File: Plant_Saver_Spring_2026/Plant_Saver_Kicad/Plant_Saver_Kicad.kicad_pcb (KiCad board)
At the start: 2 copper layers, 110 parts, among them J10 DM3D-SF, J11 Test, J2 SBH11-PBPC-D05-ST-BK, J3 SM04B-SRSS-TB, J5 Conn_01x02_Pin, J6 Conn_01x06_Socket, J7 S3B-PH-K-S, J8 54-00284, J9 1.25mm, Q1 G09P02L, Q10 G09P02L, Q11 ISP12DP06NMXTSA1, Q12 G09P02L, Q2 G09P02L, Q3 ISP12DP06NMXTSA1, Q4 G09P02L, Q5 G09P02L, Q6 G09P02L, Q7 G09P02L, Q8 G09P02L, Q9 G09P02L, SW1 Reset, SW2 25336NA, SW3 Boot, SW4 SA72SB0, U1 CDBA140SL-HF, U10 DW03C, U11 CDBA140SL-HF, U12 LP38511TJ-ADJ/NOPB, U13 MCP73833-xxx-UN, U14 MCP6234, U15 MCP73833-xxx-UN, U16 MCP6547T_I_MS, U2 CDBA140SL-HF, U3 CDBA140SL-HF, U4 CDBA140SL-HF, U5 ESP32-WROOM-32E-N16, U9 CDBA140SL-HF

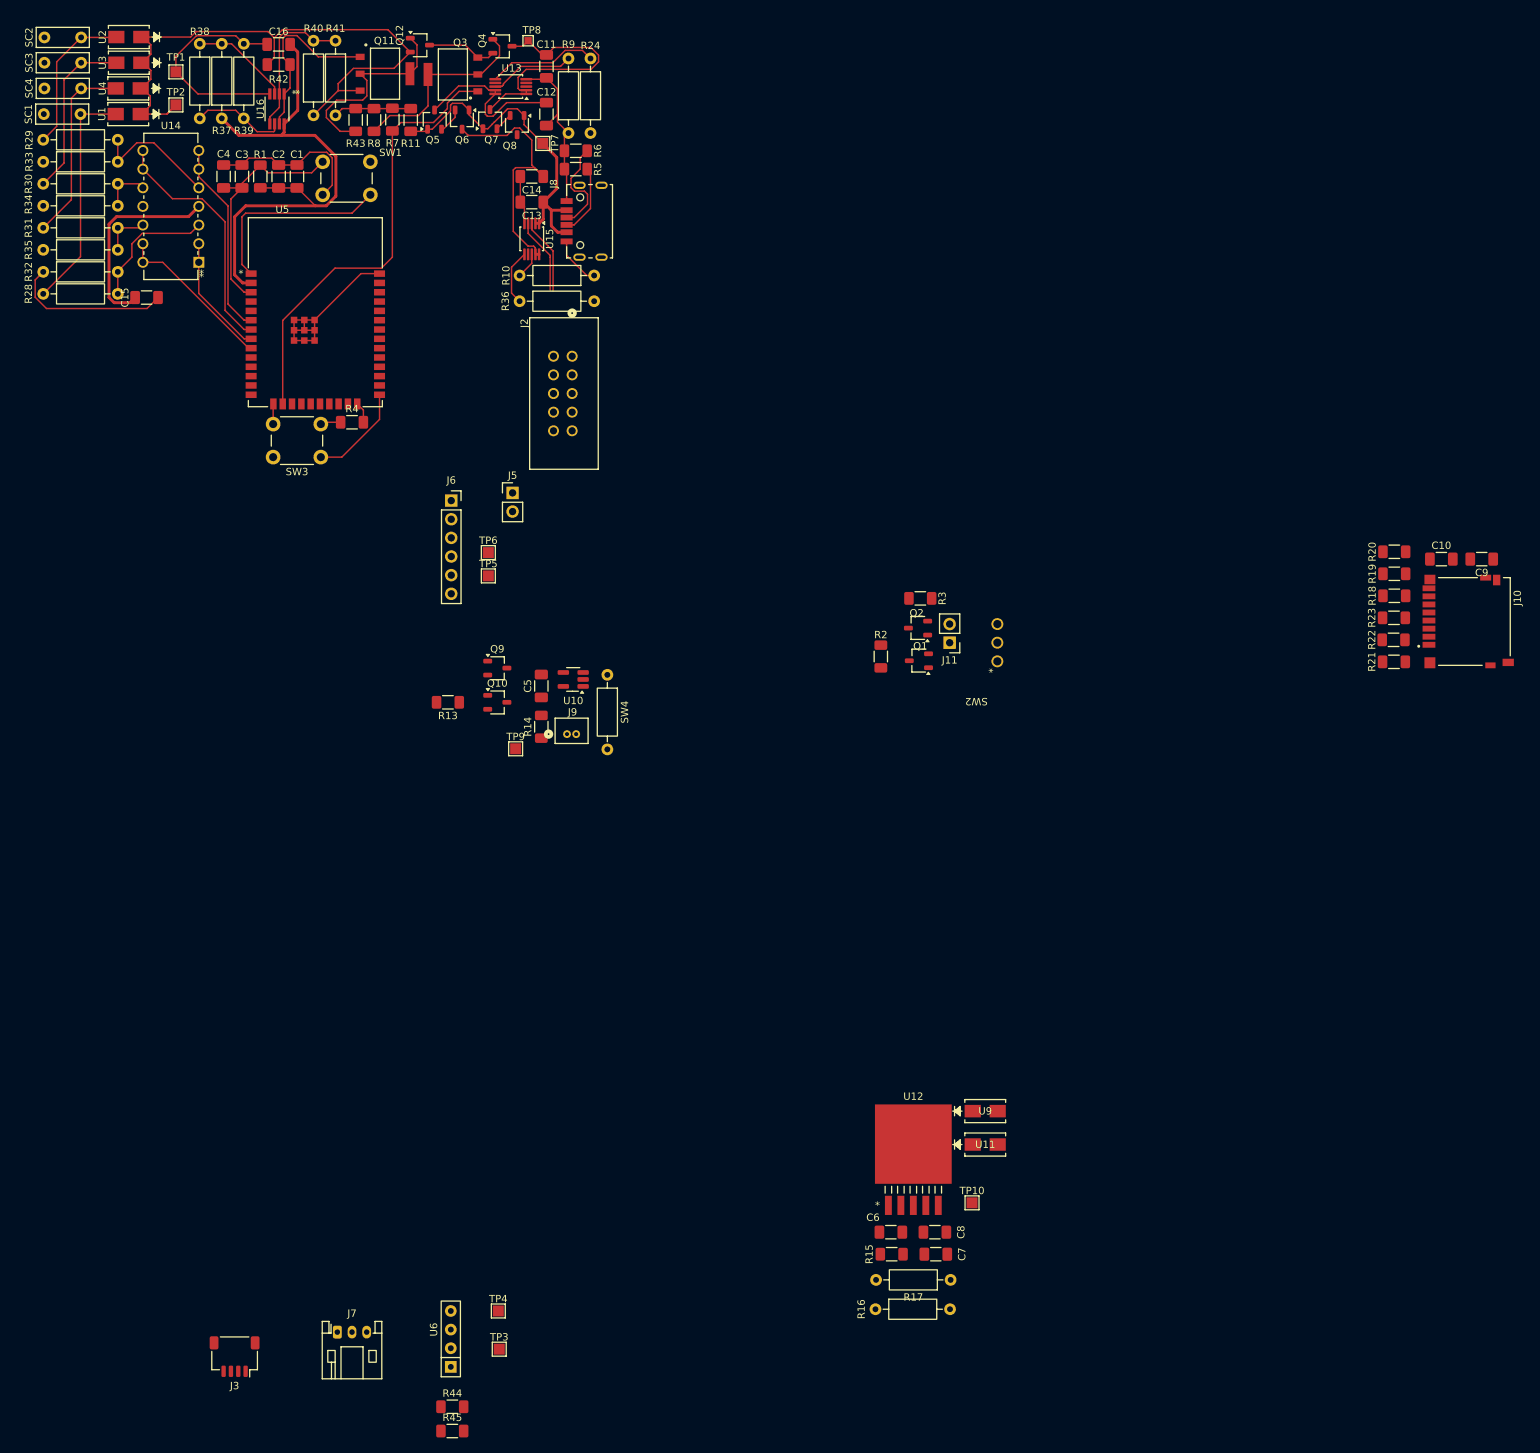
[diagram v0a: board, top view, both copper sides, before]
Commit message: Charge circuit essentially added to pcb
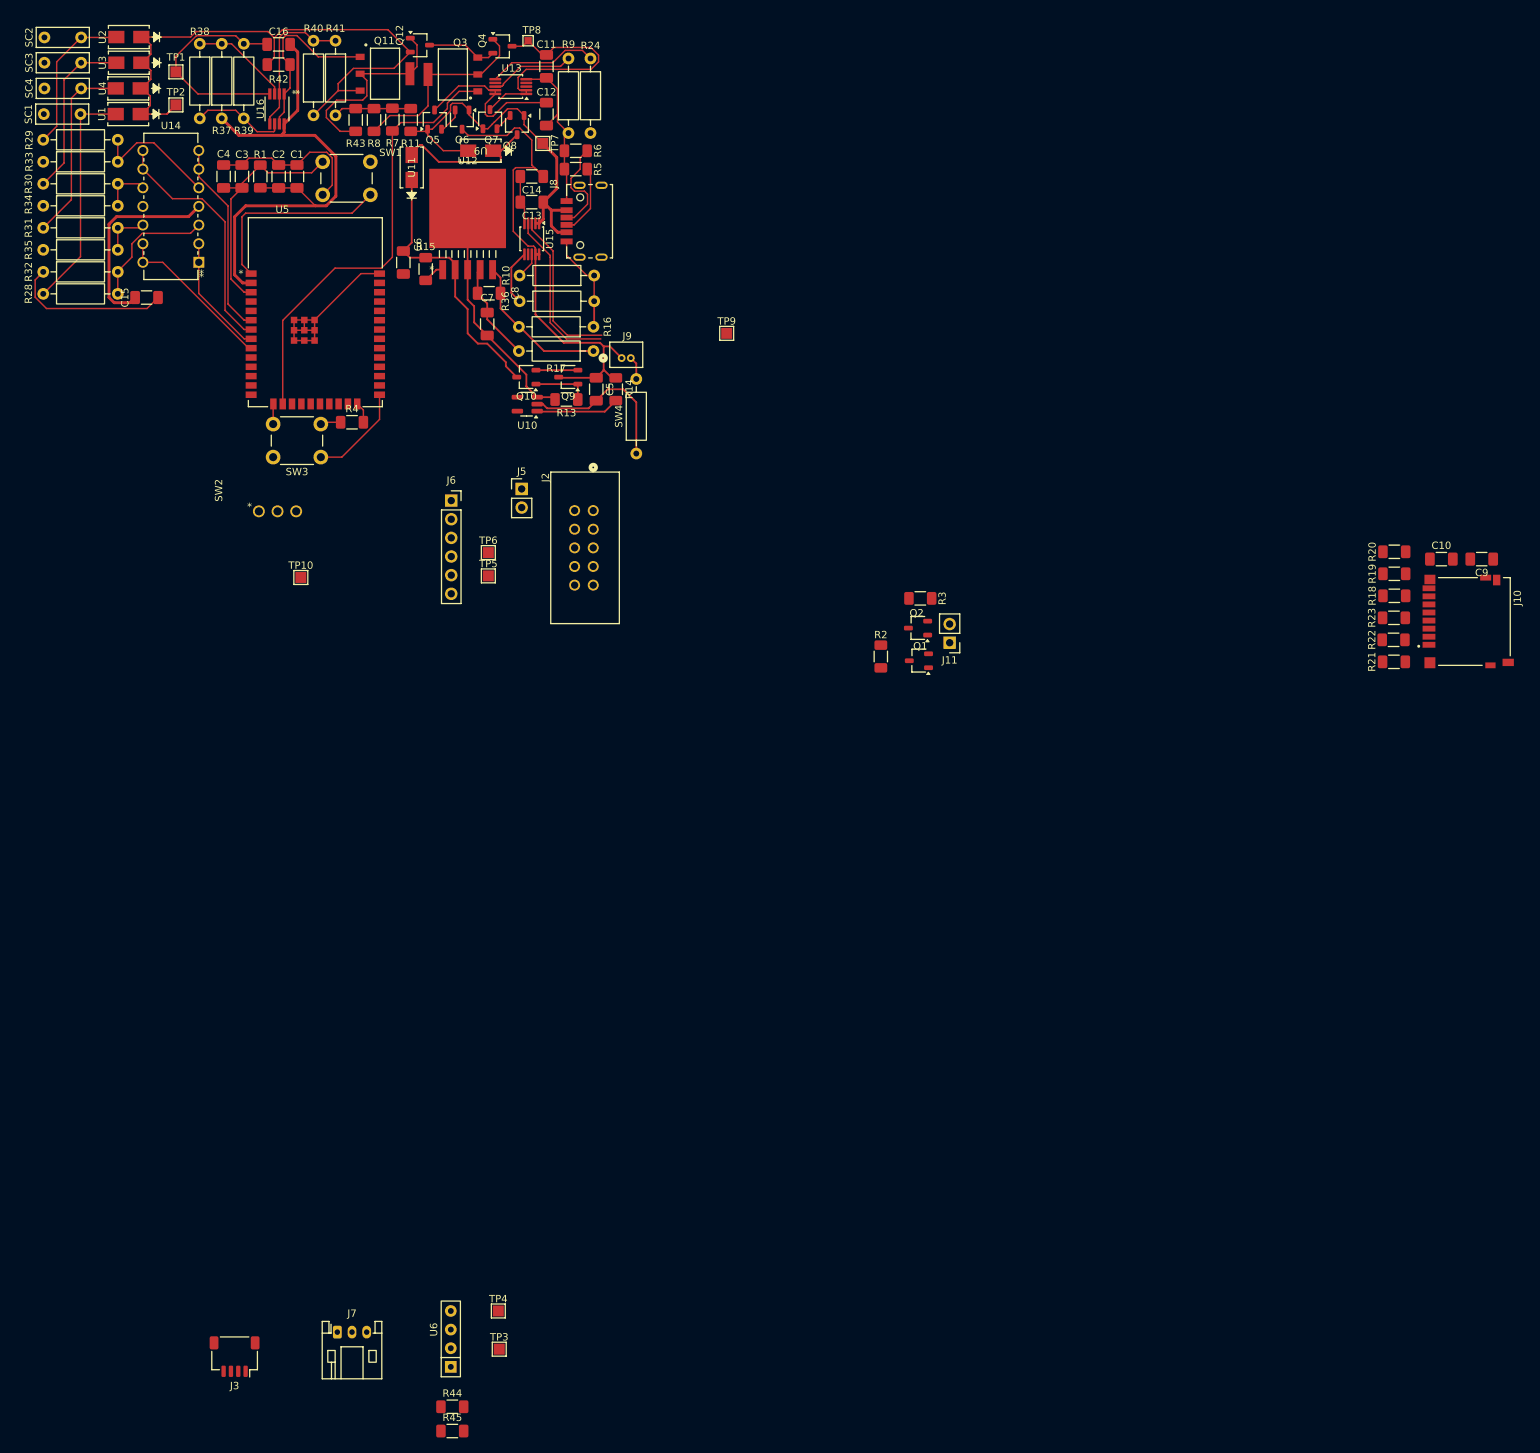
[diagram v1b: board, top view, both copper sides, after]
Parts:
- moved U11 154.4 mm to (80.1, 88.8), turned to 90 degrees
- moved R15 148.5 mm to (82.0, 102.6), turned to 90 degrees
- moved C6 147.9 mm to (79.0, 101.7), turned to -90 degrees
- moved U9 147.9 mm to (89.5, 86.5), turned to 180 degrees
- moved C8 141.7 mm to (90.7, 105.9)
- moved U12 141.2 mm to (87.8, 94.4)
- moved C7 140.7 mm to (90.4, 110.1), turned to -90 degrees
- moved R16 139.3 mm to (104.9, 110.5), turned to 180 degrees
- moved R17 135.6 mm to (104.9, 113.8)
- moved TP10 125.0 mm to (65.0, 144.7)
- moved SW2 102.7 mm to (59.3, 135.6), turned to 0 degrees
- moved TP9 63.5 mm to (123.1, 111.4)
- moved J9 51.8 mm to (108.7, 114.8)
- moved R14 47.1 mm to (108.0, 119.0), turned to -90 degrees
- moved Q10 44.5 mm to (95.8, 117.3), turned to 180 degrees
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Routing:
- net GND: track 181.2 -> 220.5 mm
- net /Power_And_Charging/Linear_Regulator/Vin: track 0.00 -> 37.6 mm
- net /Power_And_Charging/MCP73833_USB/Vbat: track 35.3 -> 69.7 mm
- net Net-(Q10-G): track 0.00 -> 27.8 mm
- net Net-(U10-GND): track 0.00 -> 22.5 mm
- net Net-(U12-ADJ): track 0.00 -> 20.8 mm
- net /Power_And_Charging/Vout: track 0.00 -> 13.6 mm
- net STAT2: track 10.4 -> 22.6 mm
- net STAT1: track 10.5 -> 22.0 mm
- net Net-(U10-Vdd): track 0.00 -> 11.4 mm
- net /Power_And_Charging/Vbus_USB: track 47.0 -> 54.2 mm
- net Net-(Q10-S): track 0.00 -> 5.72 mm
- net Net-(J9-Pad2): track 0.00 -> 3.16 mm
- net Net-(U12-EN): track 0.00 -> 2.92 mm

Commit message: Re-routed to free trapped lines
Repositioned & re-routed to free some nets and get parts within board edge (sorry Noah)
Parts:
- moved R3 65.4 mm to (86.0, 131.5), turned to 180 degrees
- moved Q1 59.0 mm to (99.7, 124.0), turned to 0 degrees
- moved Q2 52.9 mm to (100.2, 131.4)
- moved J11 52.7 mm to (102.0, 142.0)
- moved J2 43.7 mm to (69.0, 160.5)
- moved R2 39.6 mm to (110.5, 134.5), turned to 180 degrees
- moved J9 39.2 mm to (81.5, 86.5), turned to 0 degrees
- moved SW4 36.8 mm to (89.1, 98.0), turned to 180 degrees
- moved R13 35.1 mm to (86.5, 88.5)
- moved TP9 34.2 mm to (92.5, 96.0)
- moved C5 33.7 mm to (86.5, 91.0), turned to 180 degrees
- moved R14 33.3 mm to (86.5, 93.5), turned to 180 degrees
- moved U10 33.3 mm to (80.7, 91.5)
- moved Q9 31.5 mm to (91.5, 87.5), turned to 0 degrees
- moved C6 27.7 mm to (86.0, 128.5), turned to 180 degrees
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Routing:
- net SPI_MOSI: track 0.00 -> 19.6 mm
- net GND: track 220.5 -> 240.1 mm, vias 0 -> 2
- net SCL: track 0.00 -> 17.9 mm
- net Net-(J6-Pin_5): track 0.00 -> 16.7 mm
- net /Power_And_Charging/Vout: track 13.6 -> 29.0 mm
- net Net-(J6-Pin_4): track 0.00 -> 15.0 mm
- net SDA: track 0.00 -> 13.7 mm
- net /Power_And_Charging/MCP73833_USB/Vbat: track 69.7 -> 56.7 mm
- net /Power_And_Charging/Vbus_USB: track 54.2 -> 66.6 mm
- net STAT2: track 22.6 -> 10.8 mm
- net STAT1: track 22.0 -> 10.9 mm
- net SPI_MISO: track 0.00 -> 11.0 mm
- net Net-(U10-GND): track 22.5 -> 11.8 mm
- net Net-(J9-Pad2): track 3.16 -> 13.1 mm
- net SPI_CLK: track 0.00 -> 9.50 mm
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- added copper zone on B.Cu, net GND
